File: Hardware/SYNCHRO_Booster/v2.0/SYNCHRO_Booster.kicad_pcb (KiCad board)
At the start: 2 copper layers, 71.1 x 67.3 mm, 45 parts, among them IC1 L6203, J1 Conn_01x02_Pin, J2 Power_Input, J3 B4B-XH-A, SW1 SW_Push, SW2 SW_SPDT, U1 LM393P, U2 6N137, U3 6N137, U4 74LVC2G02

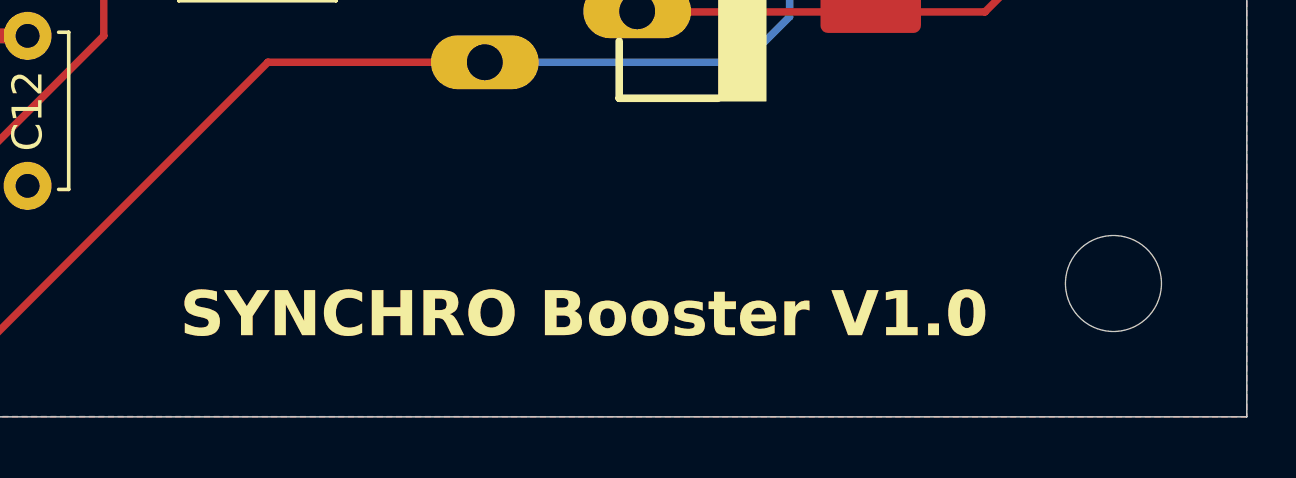
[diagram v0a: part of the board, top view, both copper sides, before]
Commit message: updating Booster PCB to V3.0 (new footprints, layout changes and current sense redesign)
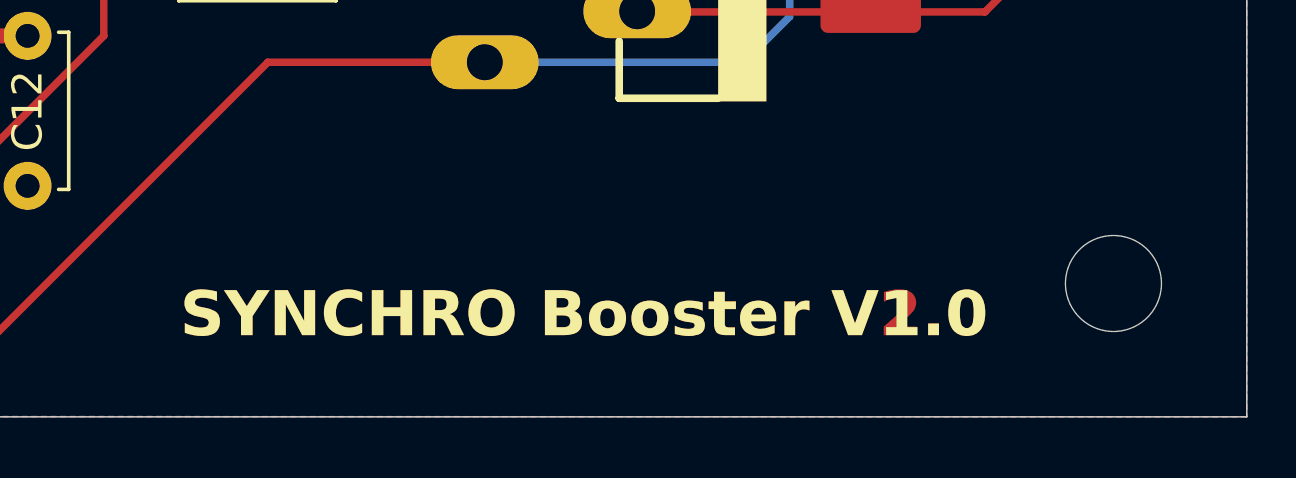
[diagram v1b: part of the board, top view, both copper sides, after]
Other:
- board text added: "100nF Kondensator Footprint wechseln"
- board text added: "SYNCHRO Booster V2.0"
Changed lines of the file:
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@@
 		(layer "Edge.Cuts")
 	)
-	(gr_text "SYNCHRO Booster V1.0"
+	(gr_text "SYNCHRO Booster V2.0"
 		(at 91.44 152.4 0)
 		(layer "F.Cu")
@@
 		)
 	)
+	(gr_text "100nF Kondensator Footprint wechseln\n"
+		(at 58 83.5 0)
+		(layer "User.1")
+		(effects
+			(font
+				(size 1.5 1.5)
+				(thickness 0.3)
+				(bold yes)
+			)
+			(justify left bottom)
+		)
+	)
